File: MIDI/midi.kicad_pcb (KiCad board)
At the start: 2 copper layers, 87 x 19.5 mm, 16 parts, among them J1 MIDI-IN, J2 MIDI_OUT, J3 MIDI-THROUGH, J4 PMOD, J5 EXT, U1 TLP2361

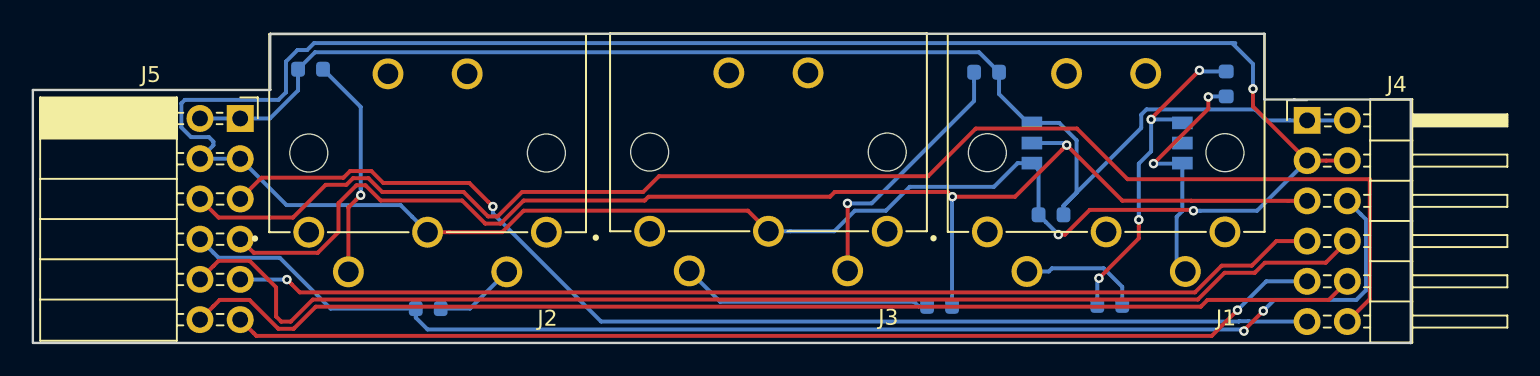
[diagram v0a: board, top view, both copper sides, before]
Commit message: Adding groundplane
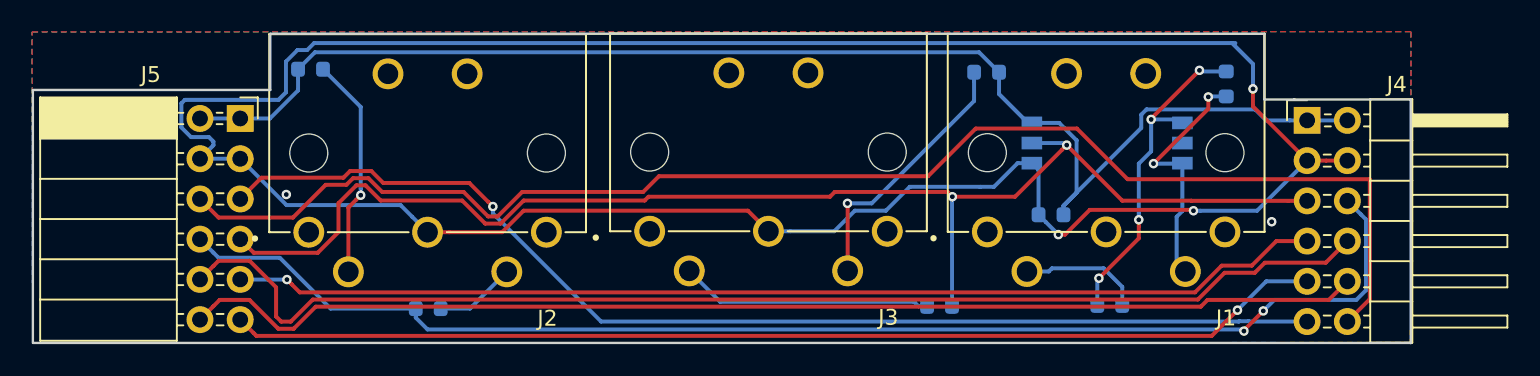
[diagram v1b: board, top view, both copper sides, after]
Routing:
- net GND: vias 3 -> 5
- added copper zone on B.Cu, net GND
- added copper zone on F.Cu, net GND
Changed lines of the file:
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@@
     (thickness 1.6)
     (drawings 22)
-    (tracks 262)
+    (tracks 265)
     (zones 0)
     (modules 16)
@@
   (segment (start 87.845003 94.799999) (end 86.545002 96.1) (width 0.25) (layer B.Cu) (net 1))
   (segment (start 99.02 91.8) (end 98.12 91.8) (width 0.25) (layer B.Cu) (net 1))
-  (segment (start 96.625002 93.294998) (end 91.309998 93.294998) (width 0.25) (layer B.Cu) (net 1))
+  (segment (start 96.625002 93.294998) (end 95.76 93.294998) (width 0.25) (layer B.Cu) (net 1))
   (segment (start 98.12 91.8) (end 96.625002 93.294998) (width 0.25) (layer B.Cu) (net 1))
   (segment (start 89.804997 94.799999) (end 87.845003 94.799999) (width 0.25) (layer B.Cu) (net 1))
@@
   (segment (start 59.159989 94.449989) (end 59.895001 95.185001) (width 0.25) (layer B.Cu) (net 1))
   (segment (start 59.895001 95.185001) (end 60.87 96.16) (width 0.25) (layer B.Cu) (net 1))
+  (via (at 114.16 95.5) (size 0.6) (drill 0.3) (layers F.Cu B.Cu) (net 1))
+  (segment (start 95.76 93.294998) (end 91.309998 93.294998) (width 0.25) (layer B.Cu) (net 1))
+  (via (at 51.95 93.78) (size 0.6) (drill 0.3) (layers F.Cu B.Cu) (net 1))
   (segment (start 98.77 89.26) (end 99.02 89.26) (width 0.25) (layer B.Cu) (net 2))
   (segment (start 96.9475 87.4375) (end 98.77 89.26) (width 0.25) (layer B.Cu) (net 2))
@@
   (segment (start 98.71 98.64) (end 100.088858 98.64) (width 0.25) (layer B.Cu) (net 17))
   (segment (start 104.7275 99.61309) (end 103.554351 98.439941) (width 0.25) (layer B.Cu) (net 17))
+  (zone (net 1) (net_name GND) (layer F.Cu) (hatch edge 0.508)
+    (connect_pads (clearance 0.508))
+    (min_thickness 0.254)
+    (fill yes (arc_segments 16) (thermal_gap 0.508) (thermal_bridge_width 0.508))
+    (polygon
+      (pts
+        (xy 122.92 103.12) (xy 35.96 103.15) (xy 35.9 83.51) (xy 122.96 83.5)
+      )
+    )
+  )
+  (zone (net 1) (net_name GND) (layer B.Cu) (hatch edge 0.508)
+    (connect_pads (clearance 0.508))
+    (min_thickness 0.254)
+    (fill yes (arc_segments 16) (thermal_gap 0.508) (thermal_bridge_width 0.508))
+    (polygon
+      (pts
+        (xy 35.9 83.51) (xy 122.95 83.5) (xy 122.95 103.15) (xy 35.93 103.14)
+      )
+    )
+  )
 )
